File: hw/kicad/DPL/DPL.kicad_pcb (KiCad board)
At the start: 2 copper layers, 96 x 89.9 mm, 46 parts, among them J0 Programer, J1 DPL1, J2 DPL2, J3 DPL3, J4 DPL4, J5 DPL5, J6 DPL6, J7 USB_B_Micro, Q1 IRF540N, Q2 IRF540N, Q3 IRF540N, Q4 IRF540N, Q5 IRF540N, Q6 IRF540N, SW1 SW_Reed, SW2 SW_Reed, SW3 SW_Reed, SW4 SW_Reed, SW5 SW_Reed, SW6 SW_Reed, U0 SAMD21E, U1 Payload, U2 AP7215-33YG-13, Y1 32.768kHz

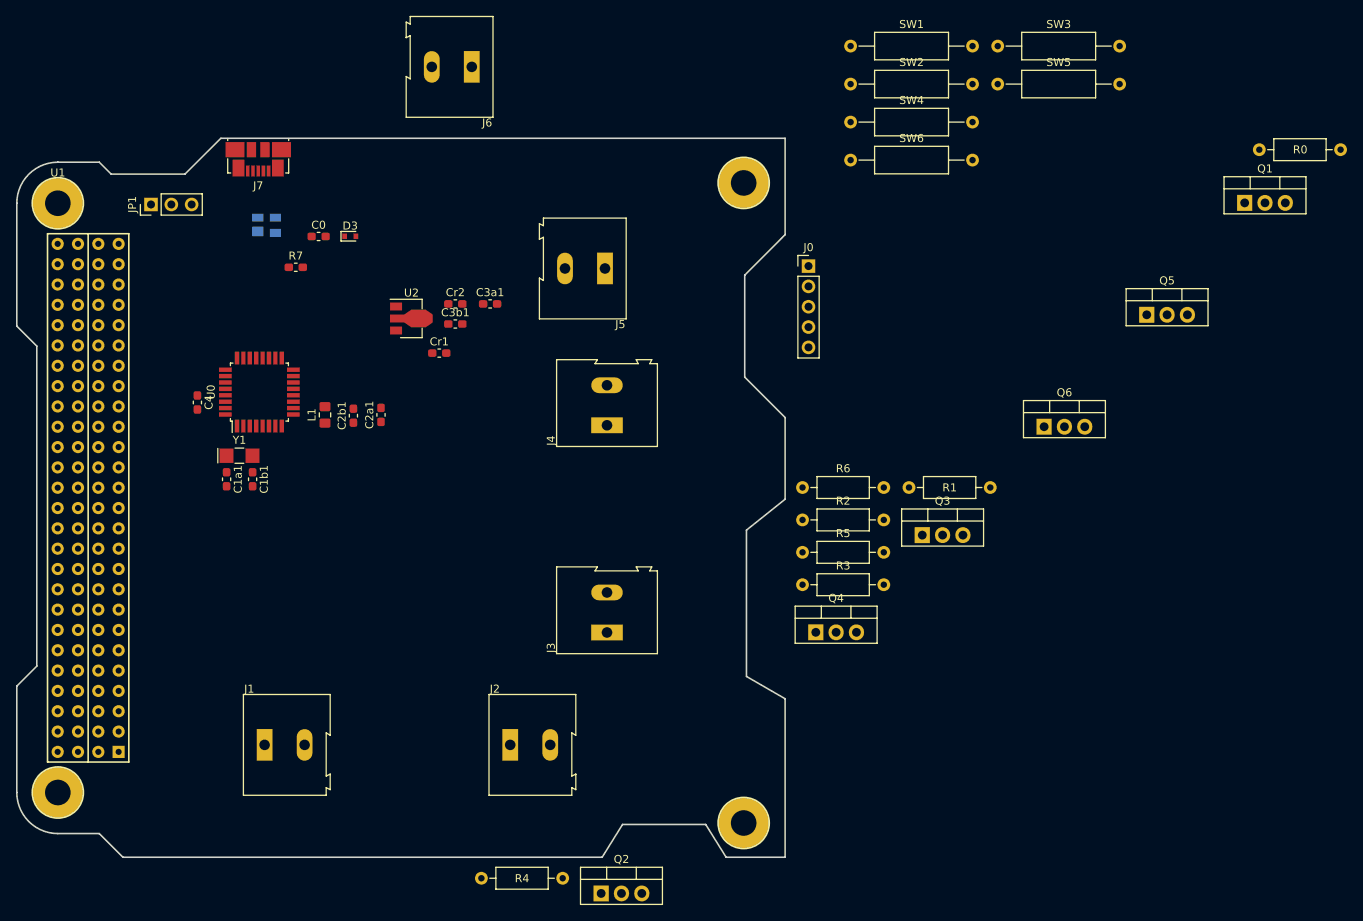
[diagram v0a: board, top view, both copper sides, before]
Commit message: Fixed some conections errors. Designed the footprint. Added vias to pass the thread wire of the balloons through them.
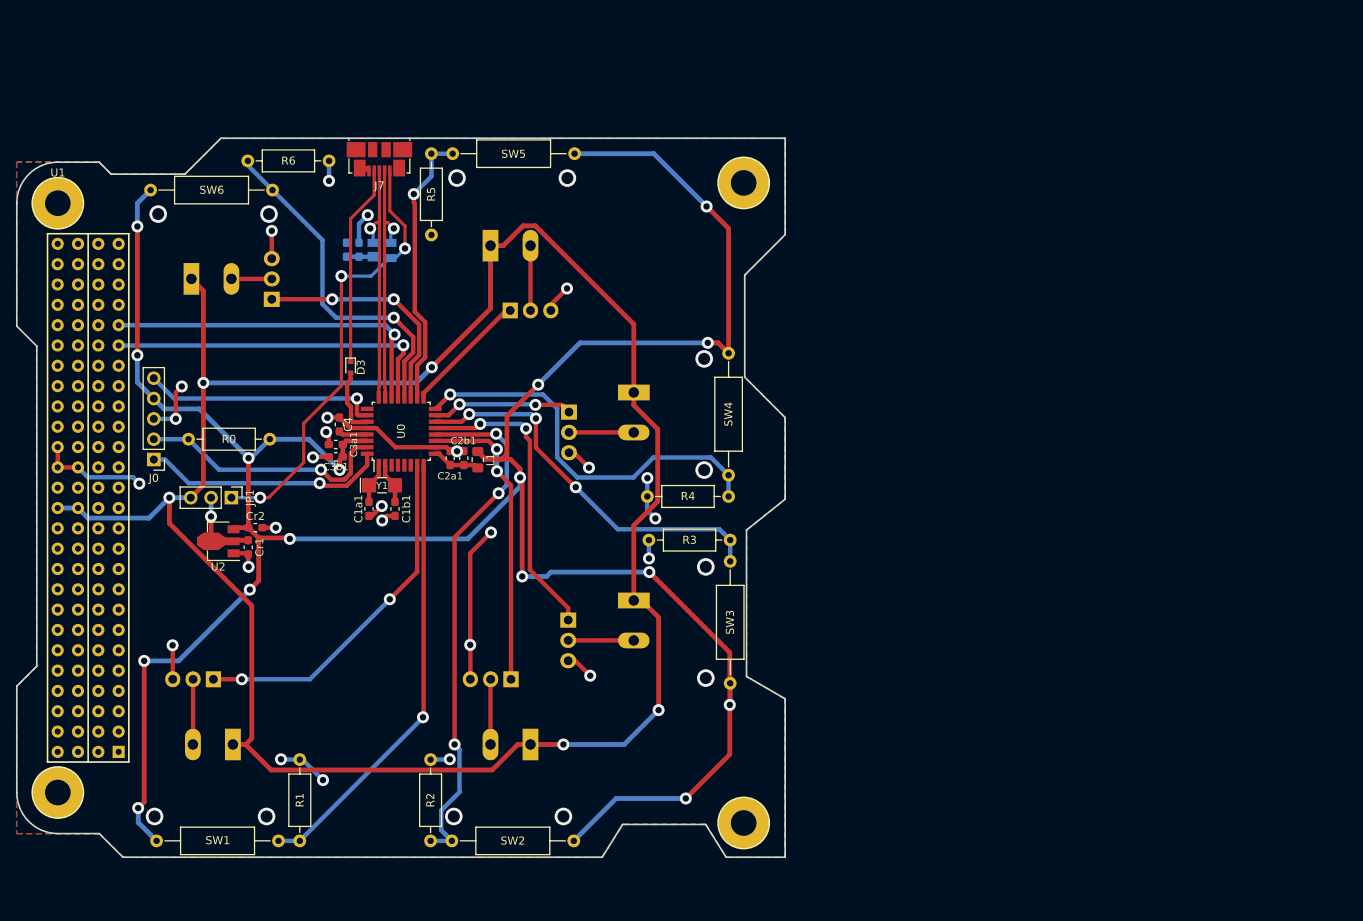
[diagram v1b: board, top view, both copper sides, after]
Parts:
- C0, J1, J2, J3, J4, J5, J6, Q1, Q2, Q3, Q4, Q5, Q6, R7: moved to B.Cu
- moved Q1 142.0 mm to (99.5, 114.8), turned to 180 degrees
- moved SW1 131.9 mm to (92.3, 135.1)
- moved R0 128.9 mm to (106.5, 84.8), turned to 180 degrees
- moved SW2 100.7 mm to (144.5, 135.1), turned to 180 degrees
- moved Q6 97.8 mm to (106.8, 67.3), turned to 90 degrees
- moved R1 88.0 mm to (110.2, 135.1), turned to 90 degrees
- moved SW6 87.6 mm to (91.6, 53.7)
- moved SW3 86.4 mm to (164.1, 115.3), turned to 90 degrees
- moved J0 85.3 mm to (92.0, 87.4), turned to 180 degrees
- moved R6 80.5 mm to (103.8, 50.0)
- moved Q5 79.6 mm to (136.6, 68.8)
- moved R5 68.1 mm to (126.7, 49.1), turned to 270 degrees
- moved R2 61.4 mm to (126.6, 135.1), turned to 90 degrees
- moved R4 56.9 mm to (163.8, 92.0), turned to 180 degrees
- moved SW5 53.6 mm to (144.6, 49.1), turned to 180 degrees
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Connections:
- net /USB_DM renamed /USB_DN
- C3a1 pad 1: GND -> /3V3
- C3b1 pad 1: GND -> /3V3
- Cr2 pad 1: GND -> /3V3
- J0 pad 4: GND -> /3V3
- L1 pad 2: GND -> /3V3
- R0 pad 1: GND -> /3V3
- SW1 pad 1: GND -> /3V3
- SW2 pad 1: GND -> /3V3
- SW3 pad 1: GND -> /3V3
- SW3 pad 2: Net-(SW3-Pad2) -> /DPL_STATUS3
- SW4 pad 1: GND -> /3V3
- SW5 pad 1: GND -> /3V3
- SW6 pad 1: GND -> /3V3
- U0 pad 30: GND -> /3V3
- U2 pad 3: GND -> /3V3
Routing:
- net /3V3: track 0.00 -> 326.7 mm, vias 0 -> 16
- net /5V0: track 0.00 -> 264.1 mm, vias 0 -> 5
- net GND: track 0.00 -> 114.1 mm, vias 0 -> 26
- net /DPL_STATUS2: track 0.00 -> 66.2 mm, vias 0 -> 3
- net /DPL_STATUS1: track 0.00 -> 56.0 mm, vias 0 -> 1
- net /VBUS: track 0.00 -> 56.0 mm, vias 0 -> 3
- net /DPL_STATUS4: track 0.00 -> 49.9 mm, vias 0 -> 1
- net /DPL_STATUS3: track 0.00 -> 48.6 mm, vias 0 -> 3
- net /EN_DPL1: track 0.00 -> 44.4 mm, vias 0 -> 2
- net /SCL: track 0.00 -> 43.0 mm, vias 0 -> 1
- net /DPL_STATUS6: track 0.00 -> 42.8 mm, vias 0 -> 1
- net /SDA: track 0.00 -> 42.4 mm, vias 0 -> 1
- net /EN_DPL3: track 0.00 -> 37.9 mm, vias 0 -> 2
- net /EN_DPL2: track 0.00 -> 37.6 mm, vias 0 -> 2
- net /DPL_STATUS5: track 0.00 -> 35.0 mm, vias 0 -> 1
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- added copper zone on B.Cu, net GND
- added copper zone on F.Cu, net GND
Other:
- net class Default: trace_width 0.25 -> 0.55; via_dia 0.8 -> 1.5; via_drill 0.4 -> 0.8
- net class Power added: clearance 0.2, trace_width 0.6, via_dia 1.5, via_drill 0.8
- net class USB added: clearance 0.2, trace_width 0.4, via_dia 1.5, via_drill 0.8

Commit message: Adding level shifter.
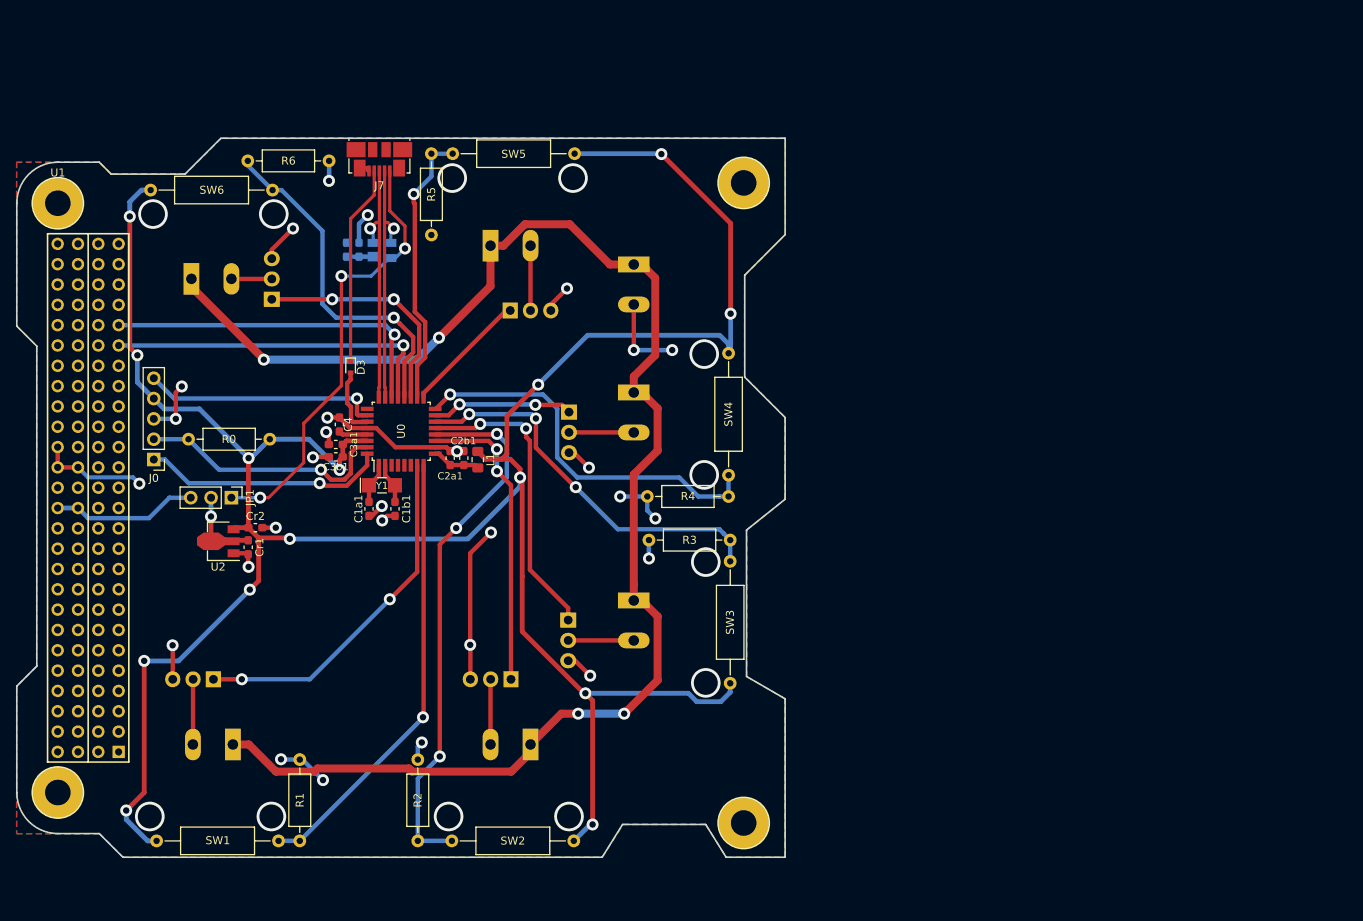
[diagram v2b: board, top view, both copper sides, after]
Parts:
- added J8: BATT, TerminalBlock:TerminalBlock_Altech_AK300-2_P5.00mm, B.Cu at (152.0, 63.0)
- moved R2 1.60 mm to (125.0, 135.1)
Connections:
- J1 pad 1: /5V0 -> /VBATT
- J2 pad 1: /5V0 -> /VBATT
- J3 pad 1: /5V0 -> /VBATT
- J4 pad 1: /5V0 -> /VBATT
- J5 pad 1: /5V0 -> /VBATT
- J6 pad 1: /5V0 -> /VBATT
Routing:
- net /5V0: track 264.1 -> 18.2 mm, vias 5 -> 0
- net /VBATT: track 0.00 -> 191.9 mm, vias 0 -> 4
- net GND: track 114.1 -> 127.0 mm, vias 26 -> 28
- net /3V3: track 326.7 -> 320.6 mm, vias 16 -> 14
- net /DPL_STATUS2: track 66.2 -> 68.0 mm
- net /DPL_STATUS4: track 49.9 -> 48.9 mm
- net /DPL_STATUS6: track 42.8 -> 43.5 mm
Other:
- net class Battery added: clearance 0.2, trace_width 1, via_dia 1.5, via_drill 0.8

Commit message: Added level shifter. Increased some drill and pad sizes. Increased power track's thickness.
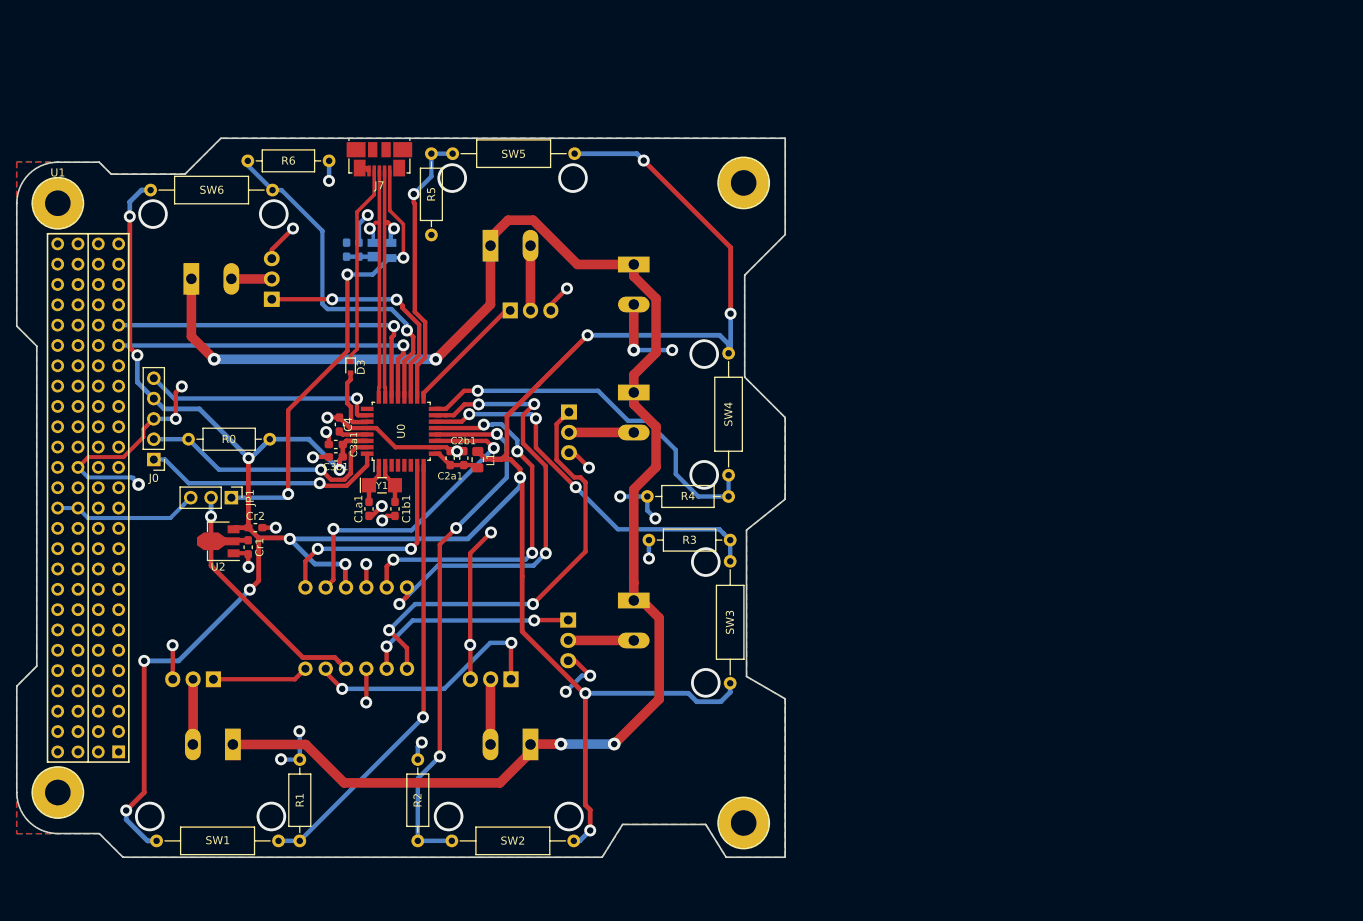
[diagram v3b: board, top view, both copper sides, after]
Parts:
- added J9: Level shifter, level:Level, B.Cu at (117.3, 108.5)
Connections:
- U0 pad 11: /EN_DPL2 -> /LV2
- U0 pad 13: /EN_DPL3 -> /LV3
- U0 pad 15: /EN_DPL4 -> /LV4
- U0 pad 7: /EN_DPL1 -> /LV1
- U1 pad : (no net) -> GND
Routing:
- net /LV4: track 0.00 -> 56.8 mm, vias 0 -> 4
- net /LV3: track 0.00 -> 47.7 mm, vias 0 -> 4
- net /LV2: track 0.00 -> 39.8 mm, vias 0 -> 2
- net /EN_DPL4: track 17.7 -> 54.4 mm
- net /EN_DPL1: track 44.4 -> 12.0 mm, vias 2 -> 0
- net /LV1: track 0.00 -> 27.9 mm, vias 0 -> 2
- net /VIN: track 11.5 -> 36.7 mm
- net GND: track 127.0 -> 145.4 mm, vias 28 -> 31
- net /EN_DPL3: track 37.9 -> 26.9 mm
- net /3V3: track 320.6 -> 330.0 mm, vias 14 -> 15
- net /VBATT: track 191.9 -> 199.1 mm
- net /EN_DPL2: track 37.6 -> 31.5 mm
- net /DPL_STATUS4: track 48.9 -> 47.5 mm
- net /VBUS: track 56.0 -> 57.2 mm
- net /SCL: track 43.0 -> 43.5 mm
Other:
- net class Battery: trace_width 1 -> 1.2; via_dia 1.5 -> 1.6
- net class PC104 added: clearance 0.2, trace_width 0.5, via_dia 1.5, via_drill 0.8
- net class USB: trace_width 0.4 -> 0.45

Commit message: Finished the PCB design phase.
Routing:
- net GND: track 145.4 -> 153.0 mm, vias 31 -> 32
- net /VBATT: track 199.1 -> 197.1 mm
- net /VBUS: track 57.2 -> 57.8 mm
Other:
- net class Battery: trace_width 1.2 -> 1.5; via_dia 1.6 -> 1.7; via_drill 0.8 -> 0.9

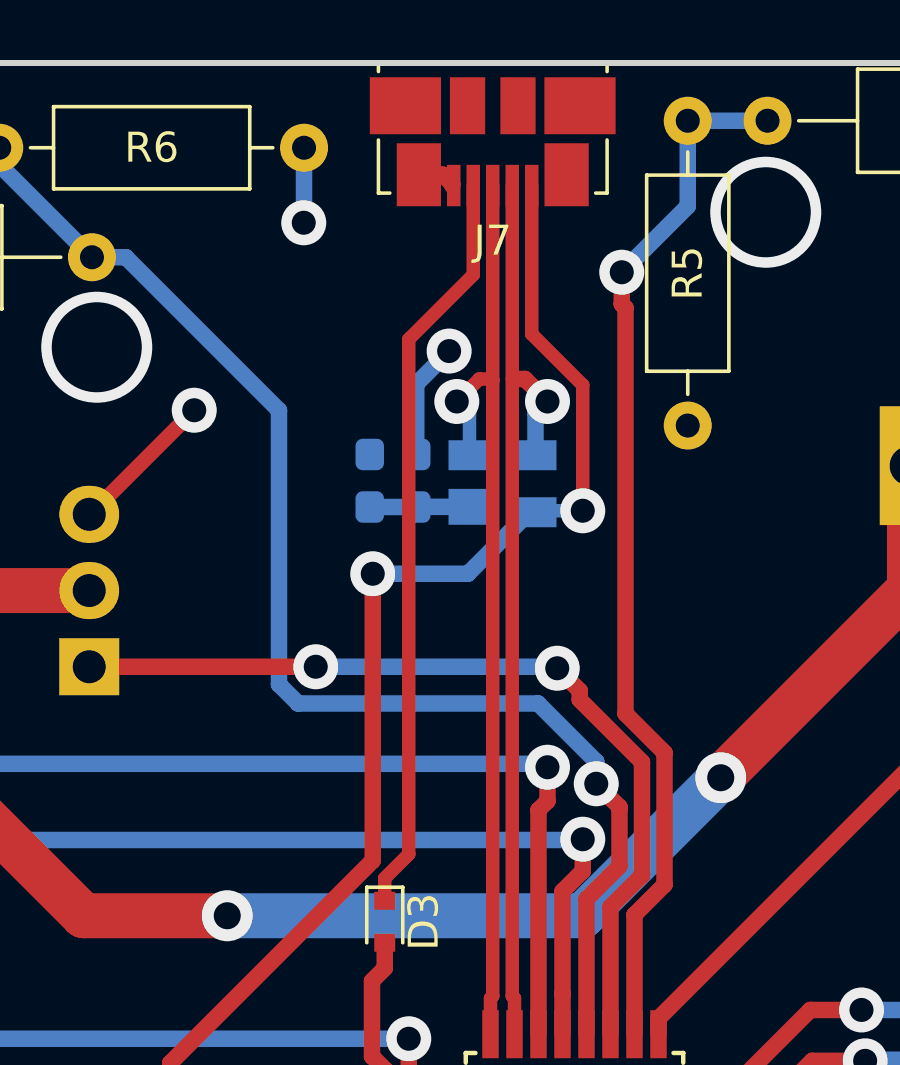
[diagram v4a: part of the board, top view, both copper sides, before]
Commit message: Improved the USB connection so that the cable doesn't act like an antenna.
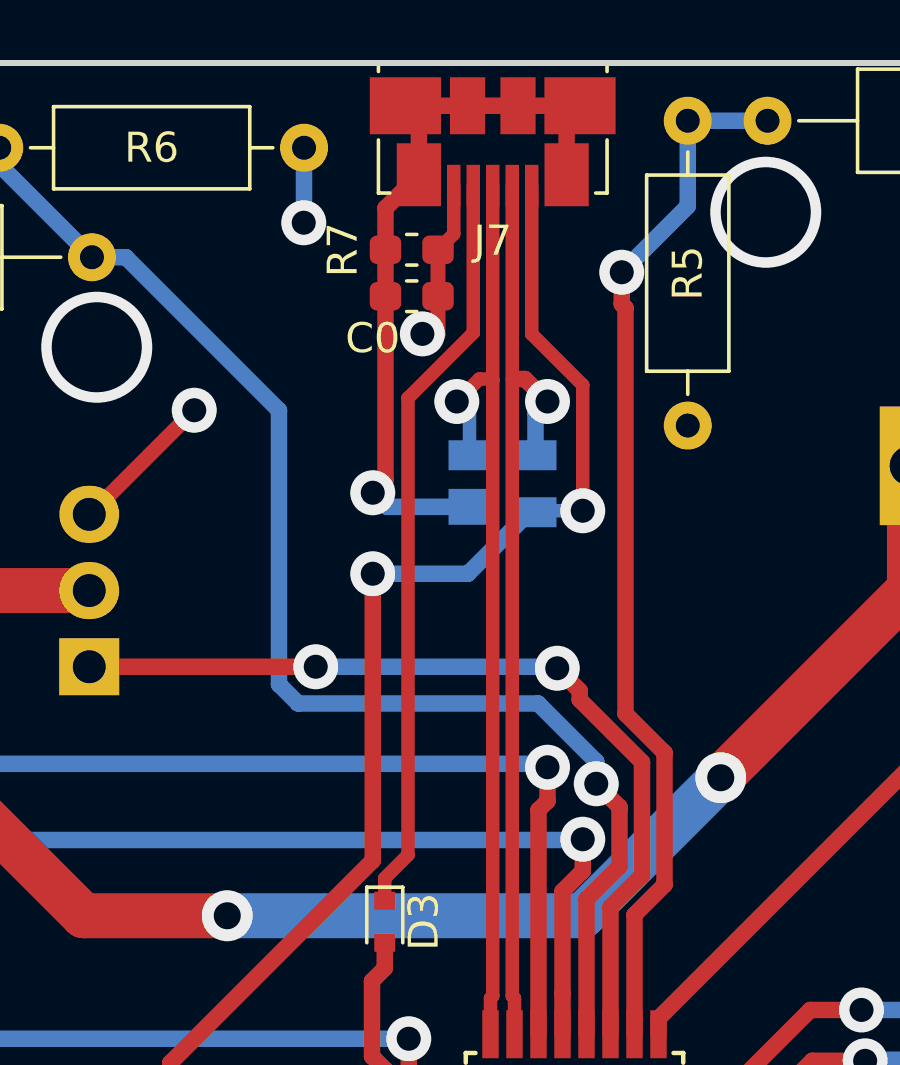
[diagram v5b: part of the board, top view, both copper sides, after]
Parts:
- C0, R7: moved to F.Cu
- moved R7 7.70 mm to (117.5, 53.5), turned to 0 degrees
- moved C0 6.31 mm to (117.5, 55.0), turned to 0 degrees
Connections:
- C0 pad 1: Net-(C0-Pad1) -> /usb/SHIELD
- D1 pad 1: Net-(C0-Pad1) -> /usb/SHIELD
- J7 pad 6: GND -> /usb/SHIELD
- R7 pad 1: Net-(C0-Pad1) -> /usb/SHIELD
- U1 pad : GND -> (no net)
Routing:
- net /usb/SHIELD: track 0.00 -> 25.4 mm, vias 0 -> 1
- net Net-(C0-Pad1): track 3.33 -> 0.00 mm
